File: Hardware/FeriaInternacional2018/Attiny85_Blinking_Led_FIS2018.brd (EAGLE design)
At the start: 50.8 x 36.5 mm, 29 parts, among them U1 ATTINY85-20P

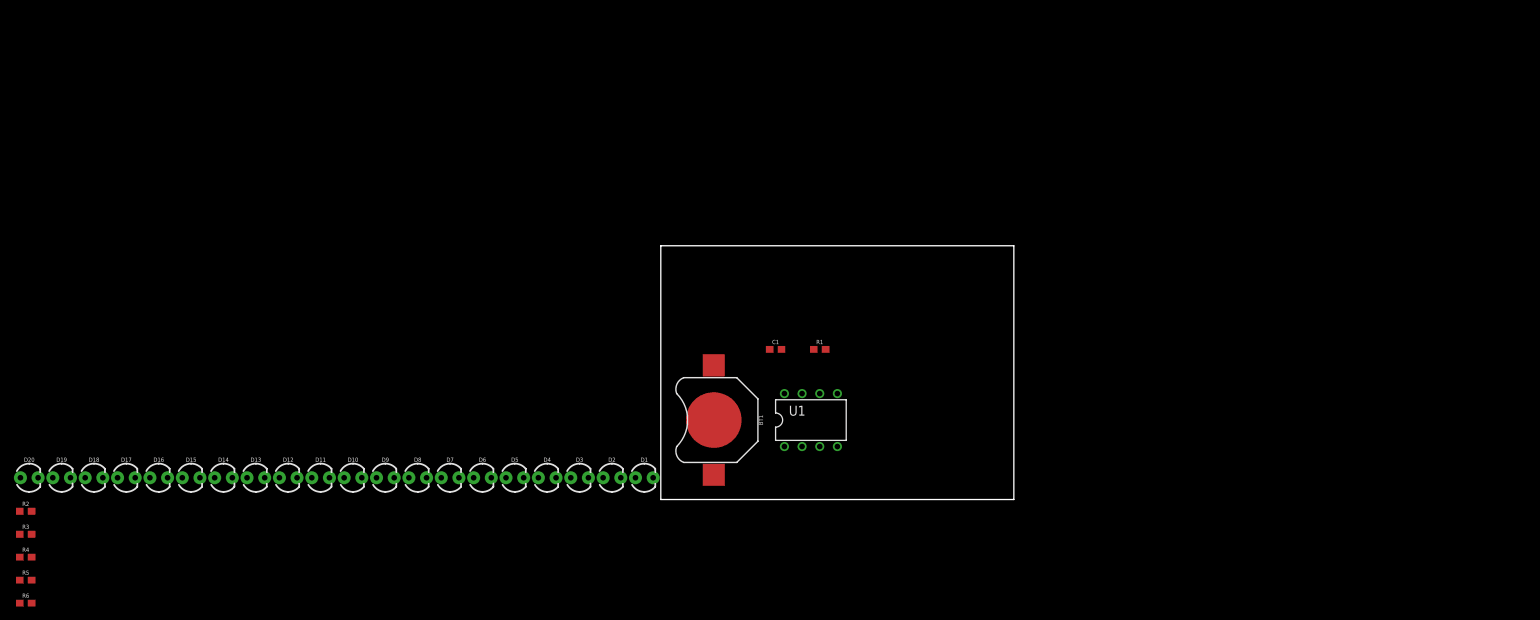
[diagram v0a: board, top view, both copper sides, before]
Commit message: Add a SPST switch, order and design a PCB circuit, doenst route yet
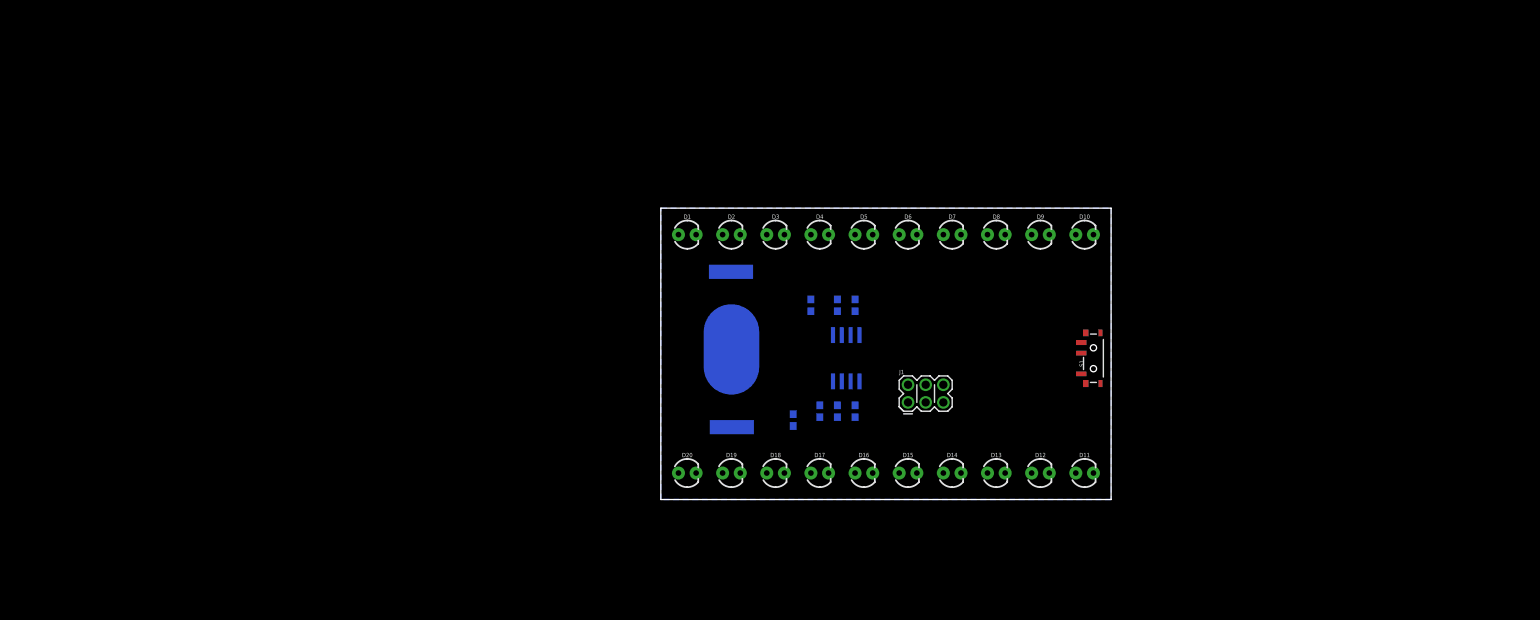
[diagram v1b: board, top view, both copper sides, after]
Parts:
- added J1: (no value), SparkFun-Connectors:2X3_POGO
- added S1: (no value), SparkFun-Switches:SWITCH_SPST_SMD_A
- BT1: device SparkFun-Batteries:BATTCON_12MM -> SparkFun-Batteries:BATTCON_20MM_4LEGS
- U1: value ATTINY85-20P -> ATTINY85-20S; device _hhn_attiny25_45_85:PDIP08_300MIL -> _hhn_attiny25_45_85:SOIC8_EIAJ_208MIL
- moved R2 122.9 mm to (27.9, 27.9), flipped to the bottom, turned to 270 degrees
- moved R6 122.4 mm to (27.9, 12.7), flipped to the bottom, turned to 270 degrees
- moved R3 121.3 mm to (25.4, 27.9), flipped to the bottom, turned to 270 degrees
- moved R5 119.2 mm to (25.4, 12.7), flipped to the bottom, turned to 270 degrees
- moved R4 116.1 mm to (22.9, 12.7), flipped to the bottom, turned to 270 degrees
- moved D10 110.9 mm to (61.0, 38.1)
- moved D11 109.9 mm to (61.0, 3.81)
- moved D12 108.2 mm to (54.6, 3.81)
- moved D13 106.5 mm to (48.3, 3.81)
- moved D14 104.8 mm to (41.9, 3.81)
- moved D15 103.1 mm to (35.6, 3.81)
- moved D16 101.4 mm to (29.2, 3.81)
- moved D9 100.5 mm to (54.6, 38.1)
- moved D17 99.7 mm to (22.9, 3.81)
- moved D18 98.0 mm to (16.5, 3.81)
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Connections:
- new net N$2: BT1.POSITIVE@1, BT1.POSITIVE@2, BT1.POSITIVE@3, BT1.POSITIVE@4, S1.2
- net GND: now also BT1.NEGATIVE; no longer BT1.GND
- net VCC: now also S1.3; no longer BT1.PWR@1
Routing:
- added copper zone on layer 16, net GND
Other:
- board size 50.8 x 36.5 mm -> 64.8 x 41.9 mm

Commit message: Disenño de placa, posicion de componentes y ruteo de lineas
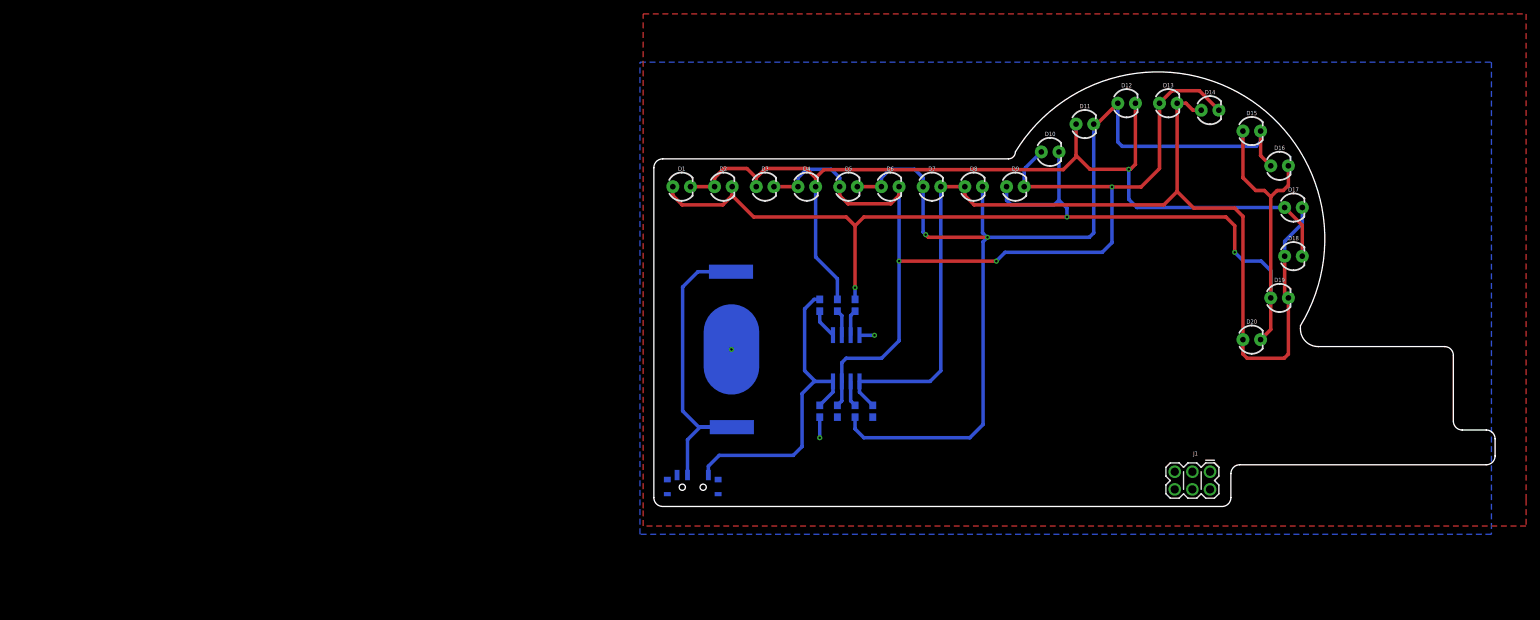
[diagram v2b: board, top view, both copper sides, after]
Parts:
- moved D20 83.4 mm to (85.0, 23.0)
- moved D19 82.8 mm to (89.0, 29.0)
- moved D18 80.8 mm to (91.0, 35.0)
- moved D17 78.1 mm to (91.0, 42.0)
- moved D16 74.3 mm to (89.0, 48.0)
- moved D15 69.7 mm to (85.0, 53.0)
- moved D14 64.0 mm to (79.0, 56.0)
- moved S1 60.6 mm to (4.59, 1.77), flipped to the bottom, turned to 180 degrees
- moved D13 58.7 mm to (73.0, 57.0)
- moved D12 54.6 mm to (67.0, 57.0)
- moved D11 50.2 mm to (61.0, 54.0)
- moved J1 44.6 mm to (79.0, 4.00), turned to 180 degrees
- moved D10 12.9 mm to (56.0, 50.0)
- moved D9 7.79 mm to (51.0, 45.0)
- moved D8 7.63 mm to (45.0, 45.0)
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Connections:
- net IO1 renamed IO11
- net IO2 renamed IO22
- net IO3 renamed IO33
- net IO4 renamed IO44
- net IO5 renamed IO55
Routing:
- net IO11: track 0.00 -> 174.5 mm, vias 0 -> 3
- net IO44: track 0.00 -> 158.8 mm, vias 0 -> 2
- net IO55: track 0.00 -> 156.4 mm
- net IO33: track 0.00 -> 149.3 mm, vias 0 -> 3
- net IO22: track 0.00 -> 142.6 mm, vias 0 -> 1
- net N$2: track 0.00 -> 47.6 mm
- net VCC: track 0.00 -> 46.8 mm
- net GND: track 0.00 -> 4.99 mm, vias 0 -> 3
- net N$1: track 0.00 -> 4.23 mm
- added copper zone on layer 1, net GND
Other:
- board size 64.8 x 41.9 mm -> 121 x 62.5 mm
- board text added: "https://github.com/alswnet/FeriaInternacional2018Badge"

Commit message: add port spi, has a desing art, add holes for badge and pin
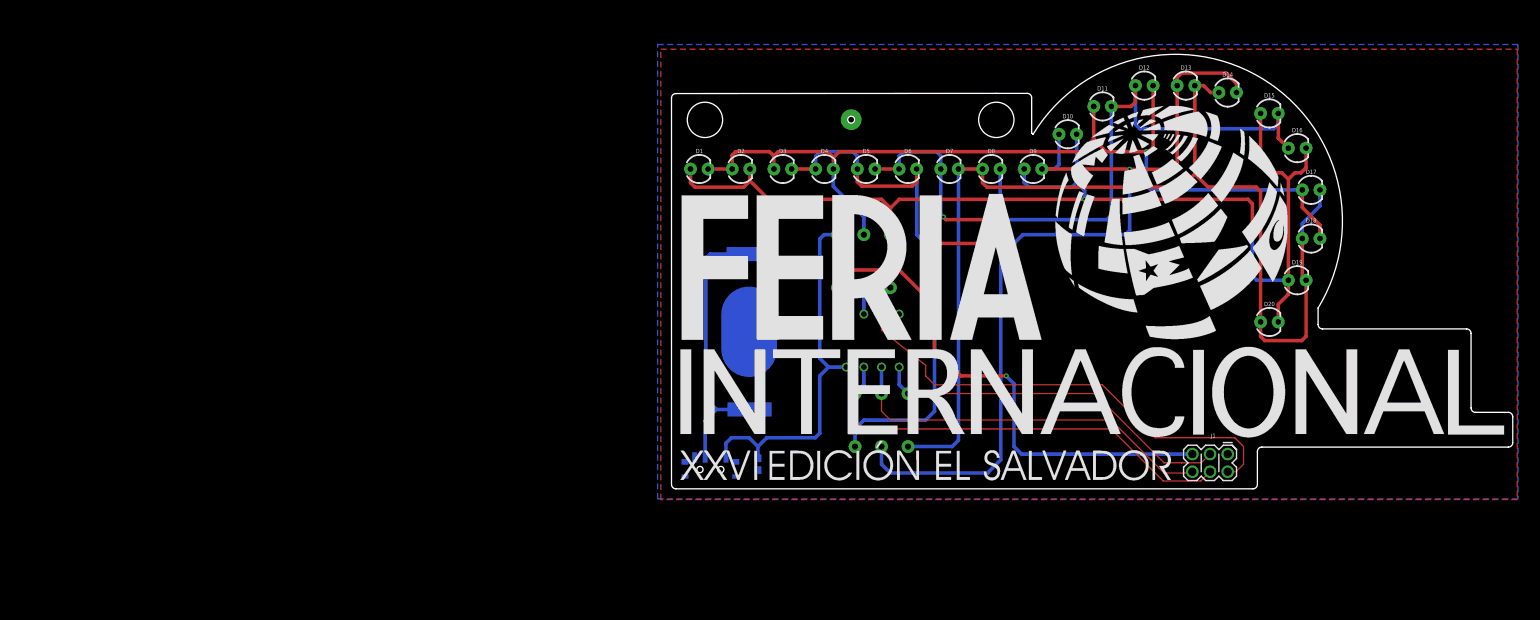
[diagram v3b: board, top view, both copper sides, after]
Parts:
- R1: device SparkFun-Resistors:0603 -> SparkFun-Resistors:AXIAL-0.3
- R2, R3, R4, R5, R6: value 1 -> 10k; device SparkFun-Resistors:0603 -> SparkFun-Resistors:AXIAL-0.3
- U1: value ATTINY85-20S -> ATTINY85-20P; device _hhn_attiny25_45_85:SOIC8_EIAJ_208MIL -> _hhn_attiny25_45_85:PDIP08_300MIL
- moved C1 11.7 mm to (14.0, 5.08)
- moved R2 8.13 mm to (33.0, 34.3)
- moved R3 7.41 mm to (29.2, 34.3)
- moved R1 6.84 mm to (25.4, 34.3)
- moved R6 5.24 mm to (35.6, 11.4), turned to 90 degrees
- moved U1 4.58 mm to (30.5, 22.9)
- moved R5 4.02 mm to (31.8, 11.4), turned to 90 degrees
- moved J1 3.59 mm to (81.5, 6.54)
- moved D12 3.59 mm to (69.5, 59.5)
- moved D13 3.59 mm to (75.5, 59.5)
- moved D14 3.59 mm to (81.5, 58.5)
- moved D15 3.59 mm to (87.5, 55.5)
- moved D16 3.59 mm to (91.5, 50.5)
- moved D17 3.59 mm to (93.5, 44.5)
- moved D18 3.59 mm to (93.5, 37.5)
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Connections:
- new net IO1: J1.P$2, R2.P$2, U1.3
- new net IO2: R3.P$2, U1.2
- new net IO3: J1.P$4, R4.P$2, U1.7
- new net IO4: J1.P$6, R5.P$2, U1.6
- new net IO5: J1.P$3, R6.P$2, U1.5
- net GND: now also J1.P$1
- net IO11: now also R2.P$1; no longer R2.1, R2.2, U1.3
- net IO22: now also R3.P$1; no longer R3.1, R3.2, U1.2
- net IO33: now also R4.P$1; no longer R4.1, R4.2, U1.7
- net IO44: now also R5.P$1; no longer R5.1, R5.2, U1.6
- net IO55: now also R6.P$1; no longer R6.1, R6.2, U1.5
- net N$1: now also R1.P$1; no longer R1.1
- net VCC: now also J1.P$5, R1.P$2; no longer R1.2
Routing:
- net VCC: track 46.8 -> 128.6 mm, vias 0 -> 1
- net IO1: track 0.00 -> 71.5 mm
- net IO3: track 0.00 -> 63.4 mm
- net IO4: track 0.00 -> 54.8 mm
- net IO5: track 0.00 -> 52.4 mm
- net IO33: track 149.3 -> 166.4 mm
- net IO22: track 142.6 -> 133.2 mm
- net IO11: track 174.5 -> 166.1 mm, vias 3 -> 2
- net IO44: track 158.8 -> 164.3 mm
- net IO55: track 156.4 -> 161.0 mm
- net IO2: track 0.00 -> 3.81 mm
- net N$2: track 47.6 -> 44.3 mm
- net GND: track 4.99 -> 5.08 mm, vias 3 -> 1
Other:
- outline, holes or cut-outs redrawn

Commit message: add logo ALSW, reorder route, redimension pcb
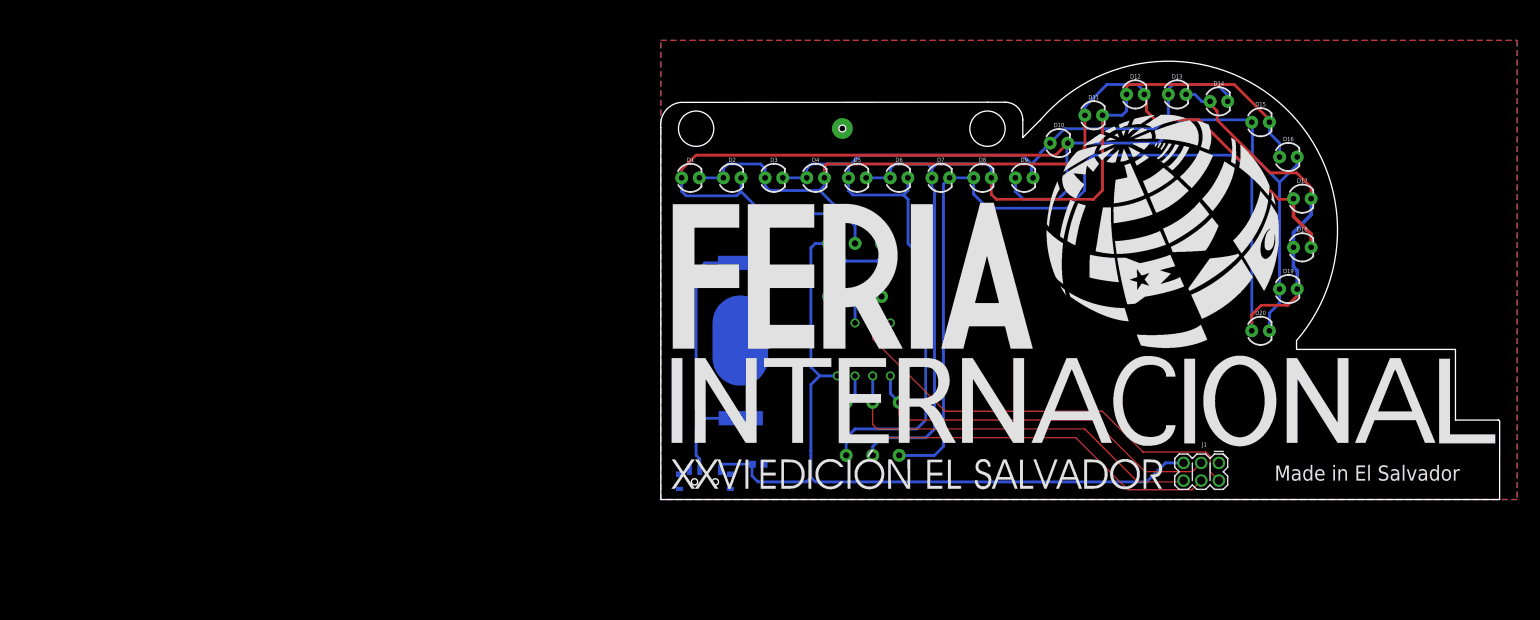
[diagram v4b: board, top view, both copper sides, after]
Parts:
- BT1: value (none) -> 3.3V
- D1, D10, D11, D12, D13, D14, D15, D16, D17, D18, D19, D2, D20, D3, D4, D5, D6, D7, D8, D9: value (none) -> RED
- J1: value (none) -> SPI
- S1: value (none) -> SWITCH
- moved S1 1.93 mm to (6.35, 2.54)
- moved J1 1.80 mm to (80.3, 5.27)
- moved D19 1.80 mm to (90.3, 30.3)
- moved D20 1.80 mm to (86.3, 24.3)
- moved D12 1.80 mm to (68.3, 58.3)
- moved D13 1.80 mm to (74.3, 58.3)
- moved D14 1.80 mm to (80.3, 57.3)
- moved D15 1.80 mm to (86.3, 54.3)
- moved D16 1.80 mm to (90.3, 49.3)
- moved D17 1.80 mm to (92.3, 43.3)
- moved D18 1.80 mm to (92.3, 36.3)
- moved R6 1.80 mm to (34.3, 10.2)
- moved BT1 1.80 mm to (11.4, 22.9)
- moved R2 1.80 mm to (31.8, 33.0)
- moved R4 1.80 mm to (26.7, 10.2)
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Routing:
- net IO44: track 164.3 -> 136.5 mm, vias 2 -> 0
- net IO33: track 166.4 -> 140.8 mm, vias 3 -> 0
- net VCC: track 128.6 -> 110.3 mm, vias 1 -> 0
- net IO11: track 166.1 -> 182.2 mm, vias 2 -> 0
- net IO55: track 161.0 -> 173.1 mm
- net IO22: track 133.2 -> 127.7 mm, vias 1 -> 0
- net IO1: track 71.5 -> 66.2 mm
- net GND: track 5.08 -> 0.00 mm, vias 1 -> 0
- net IO5: track 52.4 -> 53.5 mm
- net N$2: track 44.3 -> 44.9 mm
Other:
- board size 121 x 62.5 mm -> 120.7 x 63 mm
- board text added: "Made in El Salvador"

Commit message: Add el salvador logo, open hardware, add eschamtic attiny and isp
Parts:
- added U$1: (no value), SparkFun-Aesthetics:OSHW-LOGO-M
- added U$2: (no value), SparkFun-Aesthetics:ROHS_LOGO_0.18_IN
- R2, R3, R4, R5, R6: value 10k -> 330
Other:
- outline, holes or cut-outs redrawn
- board text added: "330"
- board text added: "Attiny85"
- board text added: "GND"
- board text added: "ISP"
- board text added: "PB0"
- board text added: "PB1"
- board text added: "PB2"
- board text added: "PB3"
- board text added: "PB4"
- board text added: "PB5"
- board text added: "Patrocinado"
- board text added: "VCC"
- board text added: "github.com/alswnet/FeriaInternacional2018Badge"
- board text added: "por: ALSW"
- board text removed: "https://github.com/alswnet/FeriaInternacional2018Badge"
